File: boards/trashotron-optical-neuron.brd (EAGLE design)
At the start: 88.9 x 50.8 mm, 17 parts, among them U1 LM358, U2 LM358, U3 LM358

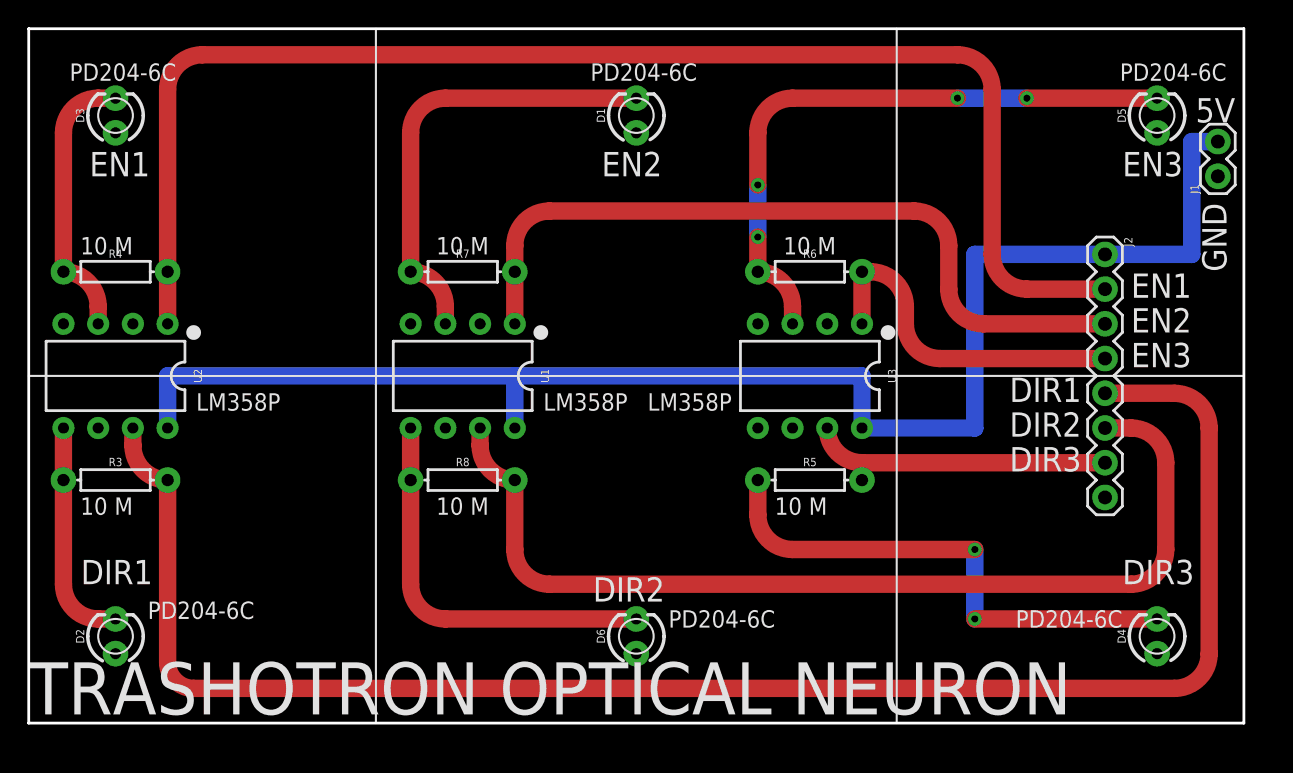
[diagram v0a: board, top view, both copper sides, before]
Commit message: this version of the boards is now all tested out on solderless breadboard
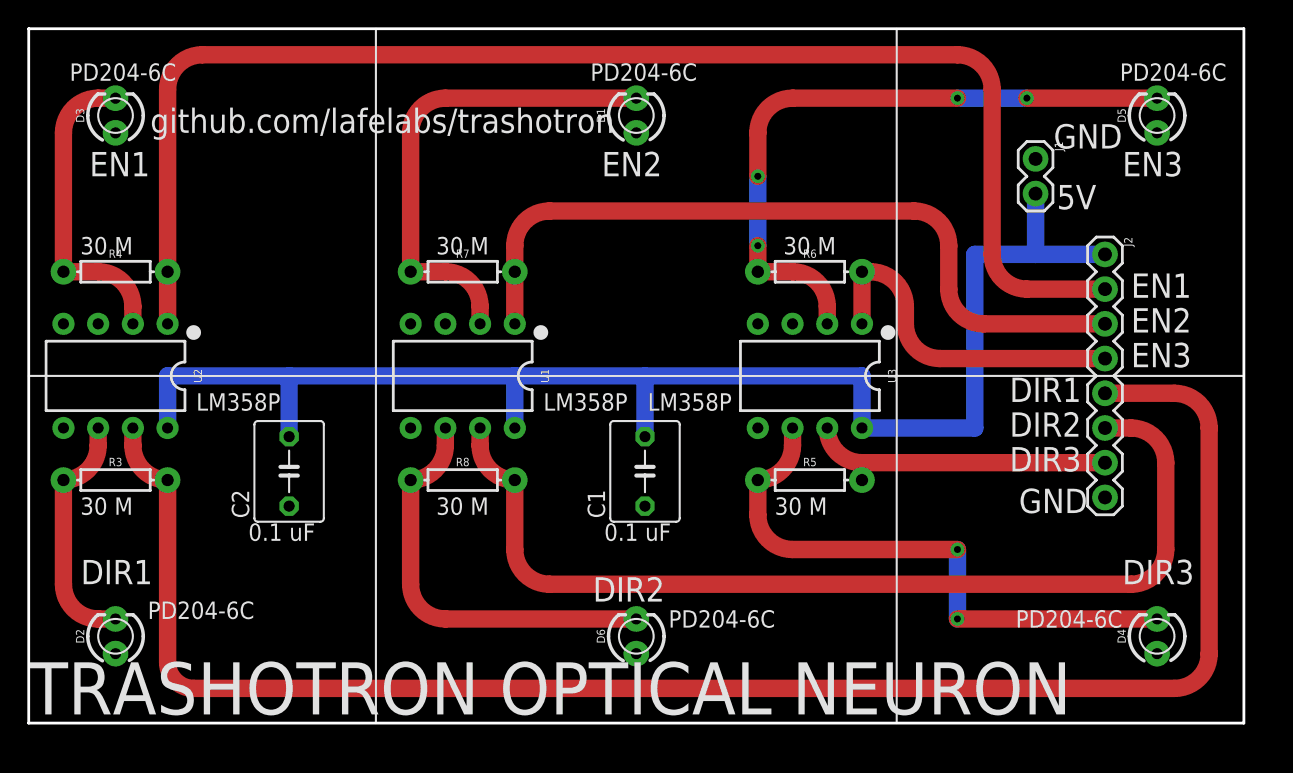
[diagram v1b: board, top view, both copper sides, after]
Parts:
- added C1, C2: (no value), rcl:C050-050X075
- moved J1 13.4 mm to (73.7, 41.3), turned to 270 degrees
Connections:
- removed net N$11: D5.K, R6.P$1, U3.3
- removed net N$13: D3.K, R4.P$1, U2.3
- removed net N$9: D4.K, R5.P$1, U3.5
- new net N$4: D3.K, R4.P$1, U2.2
- new net N$5: D2.K, R3.P$1, U2.6
- new net N$6: D4.K, R5.P$1, U3.6
- net GND: now also C1.1, C2.1, U1.3, U1.5, U2.3, U2.5, U3.3, U3.5; no longer U1.2, U1.6, U2.2, U2.6, U3.2, U3.6
- net N$1: now also U1.2; no longer U1.3
- net N$7: now also D5.K, R6.P$1, U3.2; no longer D2.K, R3.P$1, U2.5
- net N$8: now also U1.6; no longer U1.5
- net VCC: now also C1.2, C2.2
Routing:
- net N$11: track 45.3 -> 0.00 mm, vias 4 -> 0
- net N$6: track 0.00 -> 42.7 mm, vias 0 -> 2
- net N$9: track 37.9 -> 0.00 mm, vias 2 -> 0
- net N$7: track 16.3 -> 47.8 mm, vias 0 -> 4
- net N$4: track 0.00 -> 22.4 mm
- net N$13: track 19.9 -> 0.00 mm
- net N$5: track 0.00 -> 17.3 mm
- net VCC: track 109.2 -> 106.0 mm
- net N$1: track 32.6 -> 35.1 mm
- net N$8: track 29.0 -> 30.0 mm
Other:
- board text added: "0.1 uF"
- board text added: "30 M"
- board text added: "github.com/lafelabs/trashotron"
- board text removed: "10 M"
